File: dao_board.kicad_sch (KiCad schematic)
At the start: 37 parts, among them J1 KEY1, J10 DISH_SENSOR, J11 MINIBOOST_4654, J12 BATTERY, J13 DISH_LED, J2 KEY2, J3 KEY3, J4 KEY4, J5 KEY5, J6 KEY6, J7 KEY7, J8 START, J9 SELECT, SW1 SW_SPDT, SW2 HX 3x4x2-2P-1.6N, U1 XIAO-nRF52840-Plus-SMD

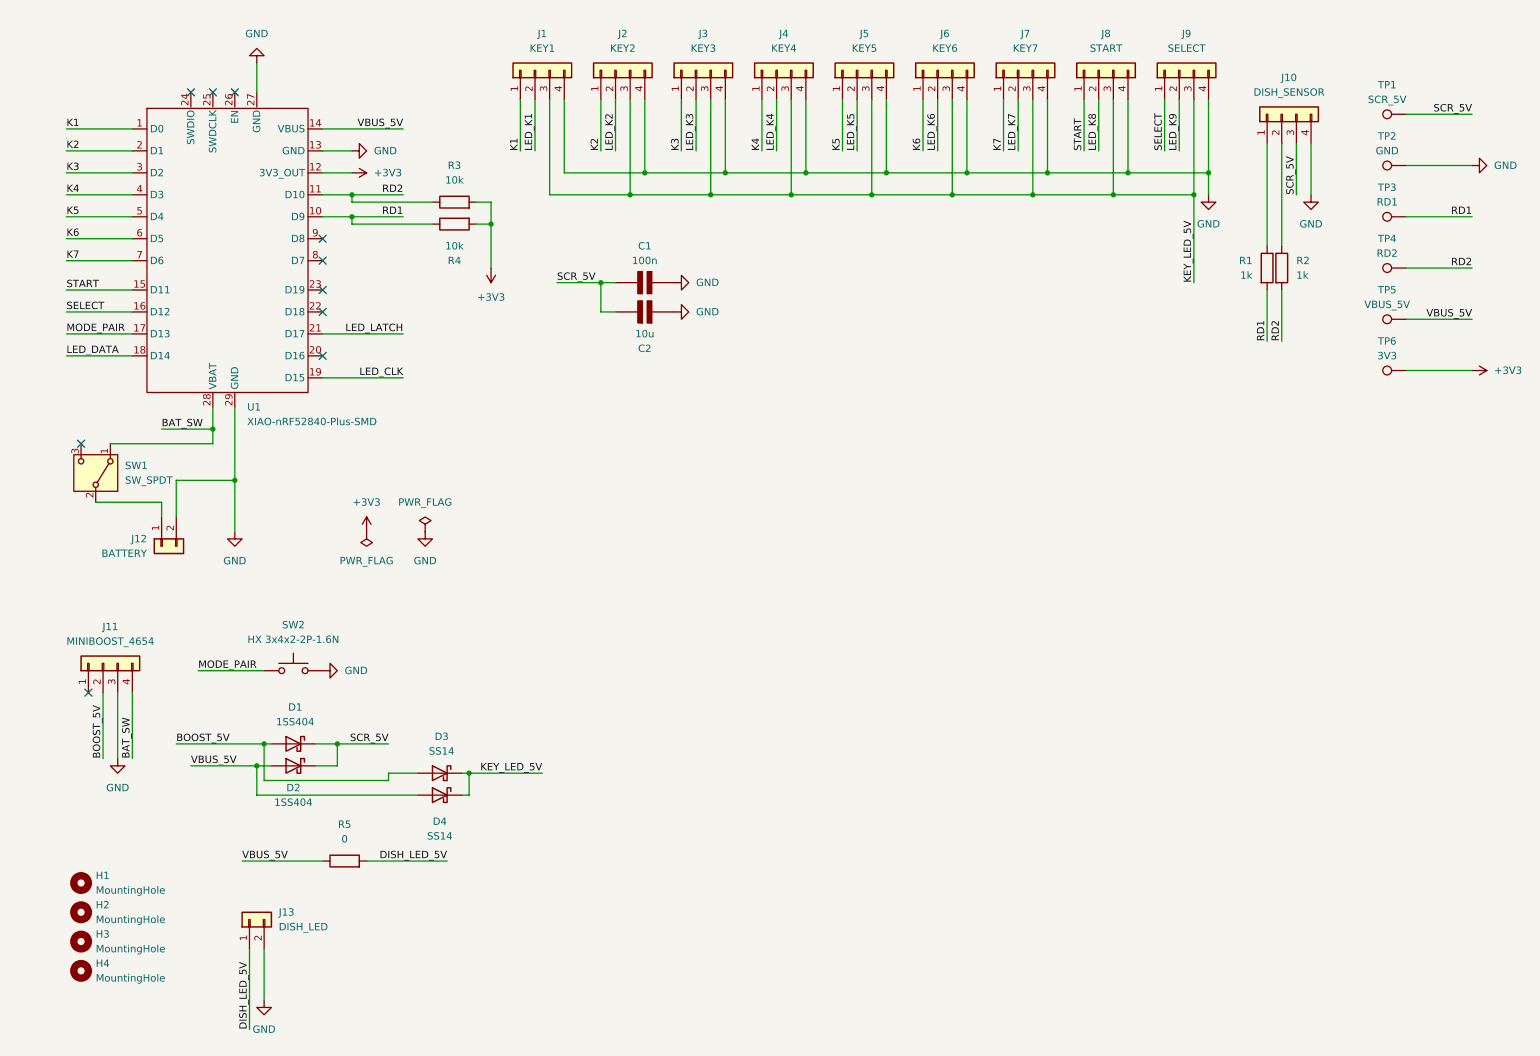
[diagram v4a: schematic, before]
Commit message: nRF52840 Plusに接続されていたものを1MV2へ移植、USB_Cシンボルの追加など
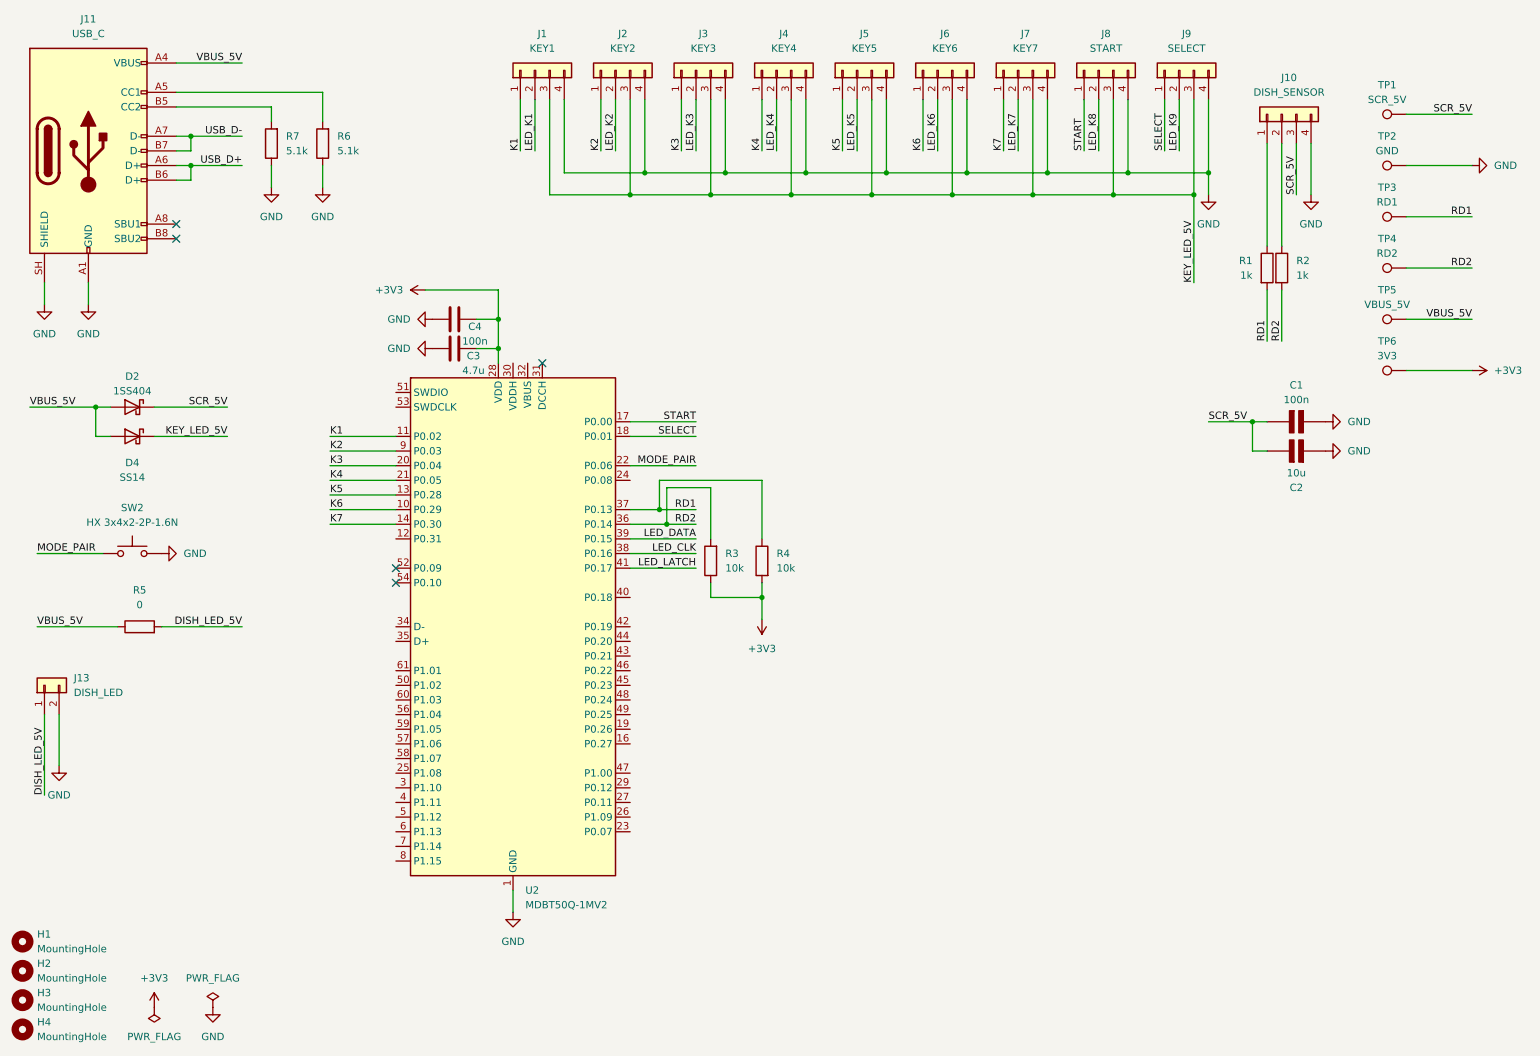
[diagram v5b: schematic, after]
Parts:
- removed D1: 1SS404, PCM_Diode_SMD_AKL:D_SOD-323, symbol Device:D_Schottky
- removed D3: SS14, PCM_Diode_SMD_AKL:D_SMA, symbol Device:D_Schottky
- removed J11: MINIBOOST_4654, Connector_PinSocket_2.54mm:PinSocket_1x04_P2.54mm_Vertical, symbol Connector_Generic:Conn_01x04
- removed J12: BATTERY, Connector_JST:JST_PH_B2B-PH-K_1x02_P2.00mm_Vertical, symbol Connector_Generic:Conn_01x02
- removed SW1: SW_SPDT, IIDXtorollerparts:SW-SMD_MK-12C02-G020, symbol Switch:SW_SPDT
- removed U1: XIAO-nRF52840-Plus-SMD, foot_one:XIAO-nRF52840-Plus-SMD, symbol Seeed_Studio_XIAO_Series:XIAO-nRF52840_Plus_SMD
- added C3: 4.7u, symbol Device:C
- added C4: 100n, symbol Device:C
- added J11: USB_C, symbol Connector:USB_C_Receptacle_USB2.0_16P
- added R6, R7: 5.1k, Library:R_0402_1005Metric, symbol Device:R
- added U2: MDBT50Q-1MV2, RF_Module:Raytac_MDBT50Q, symbol RF_Module:MDBT50Q-1MV2
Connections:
- net +3V3: now also R3.1, C3.2, C4.2, U2.28 (VDD); no longer R3.2
- net GND: now also C3.1, C4.1, J11.A1 (GND), J11.A12 (GND), J11.B1 (GND), J11.B12 (GND), J11.SH (SHIELD), R6.1, R7.1, U2.1 (GND), U2.15 (GND), U2.2 (GND), U2.33 (GND), U2.55 (GND)
- net K1: now also U2.11 (P0.02)
- net K2: now also U2.9 (P0.03)
- net K3: now also U2.20 (P0.04)
- net K4: now also U2.21 (P0.05)
- net K5: now also U2.13 (P0.28)
- net K6: now also U2.10 (P0.29)
- net K7: now also U2.14 (P0.30)
- net LED_CLK: now also U2.38 (P0.16)
- net LED_DATA: now also U2.39 (P0.15)
- net LED_LATCH: now also U2.41 (P0.17)
- net MODE_PAIR: now also U2.22 (P0.06)
- net RD1: now also U2.37 (P0.13)
- net RD2: now also R3.2, U2.36 (P0.14); no longer R3.1
- net SELECT: now also U2.18 (P0.01)
- net START: now also U2.17 (P0.00)
- net VBUS_5V: now also J11.A4 (VBUS), J11.A9 (VBUS), J11.B4 (VBUS), J11.B9 (VBUS)
- new net: J11.A5 (CC1), R6.2
- new net: J11.B5 (CC2), R7.2
- new net USB_D+: J11.A6 (D+), J11.B6 (D+)
- new net USB_D-: J11.A7 (D-), J11.B7 (D-)
- no-connect marks 10 -> 5
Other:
- moved on the sheet: C1, C2, D2, D4, H1, H2, H3, H4, J13, R5, SW2

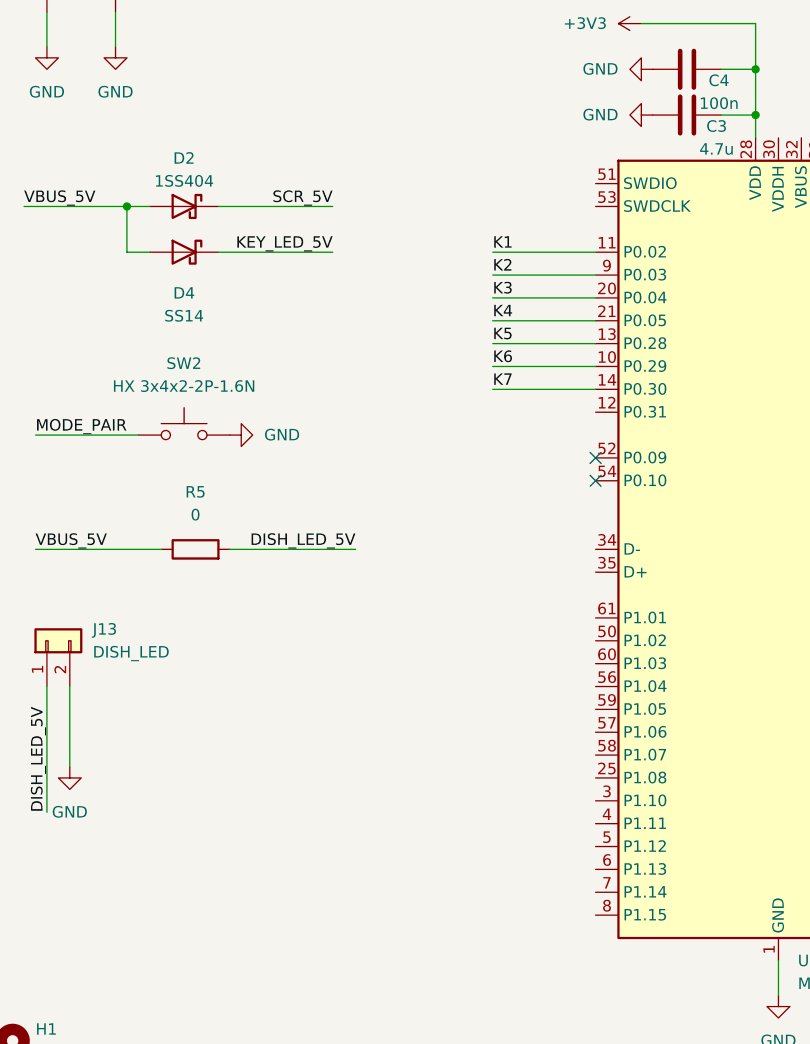
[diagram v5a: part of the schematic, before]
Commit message: 配線・フットプリント割り当ての修正、ディレクトリ内に使ったデータを追加、AIに投げるためのERCレポート保存フォルダ追加など
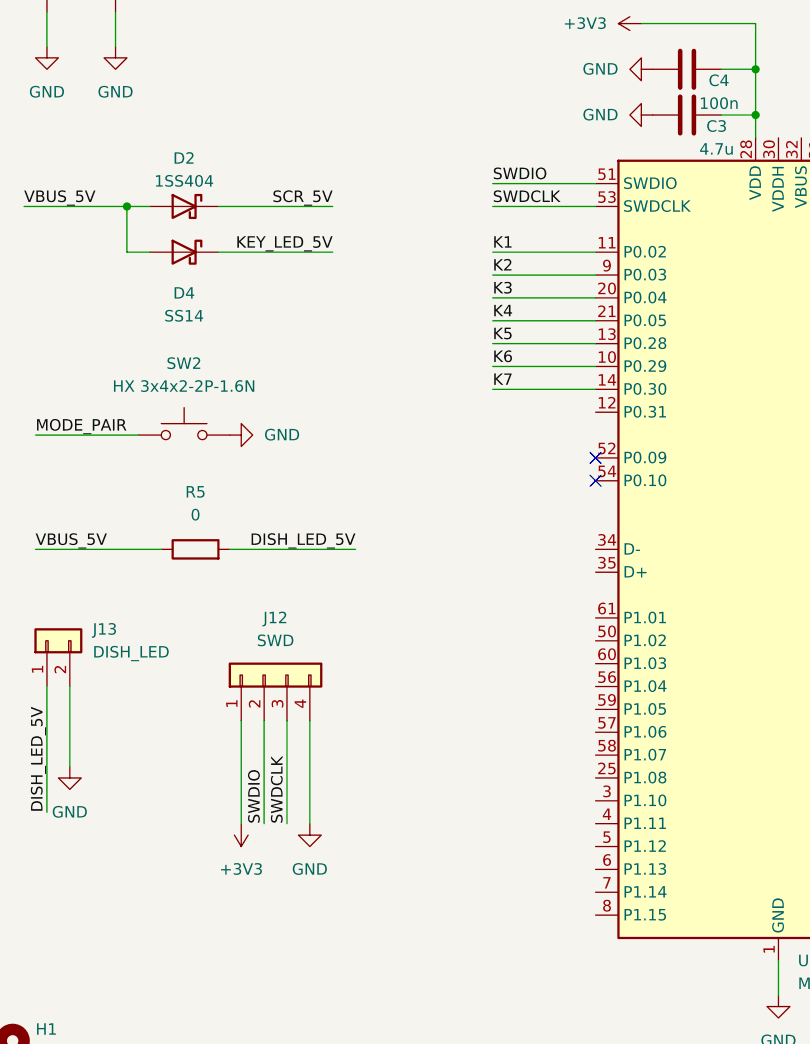
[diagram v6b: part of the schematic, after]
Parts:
- added J12: SWD, Connector:FanPinHeader_1x04_P2.54mm_Vertical, symbol Connector_Generic:Conn_01x04
- C1: footprint PCM_Capacitor_SMD_AKL:C_0402_1005Metric -> Library:C_0402_1005Metric
- C2: footprint PCM_Capacitor_SMD_AKL:C_0603_1608Metric -> Library:C_0603_1608Metric
- C3: footprint (none) -> Library:C_0603_1608Metric
- C4: footprint (none) -> Library:C_0402_1005Metric
- D2: footprint PCM_Diode_SMD_AKL:D_SOD-323 -> Library:D_SOD-323
- D4: footprint PCM_Diode_SMD_AKL:D_SMA -> Diode_SMD:D_SMA
- H1, H2, H3, H4: footprint PCM_fab:MountingHole_M5 -> Library:MountingHole_M5
- J1, J10, J2, J3, J4, J5, J6, J7, J8, J9: footprint Connector_JST:JST_XH_B4B-XH-A_1x04_P2.50mm_Vertical -> Library:JST_XH_B4B-XH-A_1x04_P2.50mm_Vertical
- J11: footprint (none) -> c165948:USB-C_SMD-TYPE-C-31-M-12_1
- J13: footprint Connector_JST:JST_XH_B2B-XH-A_1x02_P2.50mm_Vertical -> Library:JST_XH_B2B-XH-A_1x02_P2.50mm_Vertical
- R1, R2, R3, R4, R5: footprint PCM_Resistor_SMD_AKL:R_0402_1005Metric -> Library:R_0402_1005Metric
- SW2: footprint IIDXtorollerparts:KEY-SMD_L4.0-W3.0-LS4.9-1 -> Library:KEY-SMD_L4.0-W3.0-LS4.9-1
- TP1, TP2, TP3, TP4, TP5, TP6: footprint TestPoint:TestPoint_Pad_D2.0mm -> Library:TestPoint_Pad_D2.0mm
- U2: footprint RF_Module:Raytac_MDBT50Q -> c5118826:COMM-SMD_MDBT50Q-1MV2-1
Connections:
- net +3V3: now also J12.1 (Pin_1)
- net GND: now also J12.4 (Pin_4)
- net SWDIO: now reaches U2.51 (SWDIO)
- net SWDIO: now also J12.2 (Pin_2)
- net SWDCLK: now reaches U2.53 (SWDCLK)
- net SWDCLK: now also J12.3 (Pin_3)

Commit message: とりあえずリセットスイッチ用にシンボルを増やした
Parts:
- added J4: GPIO_EXPANSION, Connector_PinHeader_2.54mm:PinHeader_2x05_P2.54mm_Vertical, symbol Connector_Generic:Conn_02x05_Odd_Even
- added SW2: SW_Push, Library:KEY-SMD_L4.0-W3.0-LS4.9-1, symbol Switch:SW_Push
- renumbered C4 to C1, C3 to C2, C1 to C3, C2 to C4, D2 to D1, D4 to D2, J13 to J1, J6 to J10, J7 to J11, J8 to J12, J9 to J13, J10 to J14, J11 to J2, J12 to J3, J1 to J5, J2 to J6, J3 to J7, J4 to J8, J5 to J9, R5 to R1, R7 to R2, R6 to R3, R3 to R4, R4 to R5, R1 to R6, R2 to R7, SW2 to SW1, U2 to U1
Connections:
- net +3V3: now also J4.1 (Pin_1)
- net GND: now also J4.2 (Pin_2), SW2.2
- net USB_D+: now also U1.35 (D+)
- net USB_D-: now also U1.34 (D-)
- net EXP7: now reaches U1.19 (P0.26)
- net EXP7: now also J4.10 (Pin_10)
- net nRESET: now reaches U1.40 (P0.18)
- net nRESET: now also SW2.1
- net EXP0: now reaches U1.42 (P0.19)
- net EXP0: now also J4.3 (Pin_3)
- net EXP2: now reaches U1.43 (P0.21)
- net EXP2: now also J4.5 (Pin_5)
- net EXP1: now reaches U1.44 (P0.20)
- net EXP1: now also J4.4 (Pin_4)
- net EXP4: now reaches U1.45 (P0.23)
- net EXP4: now also J4.7 (Pin_7)
- net EXP3: now reaches U1.46 (P0.22)
- net EXP3: now also J4.6 (Pin_6)
- net EXP5: now reaches U1.48 (P0.24)
- net EXP5: now also J4.8 (Pin_8)
- net EXP6: now reaches U1.49 (P0.25)
- net EXP6: now also J4.9 (Pin_9)
- no-connect marks 5 -> 21
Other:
- moved on the sheet: C1, C2, J3, R4, R5, U1
